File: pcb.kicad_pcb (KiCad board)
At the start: 4 copper layers, 65 x 56 mm, 28 parts, among them J1 230VAC IN, J10 DHT22 2, J11 DHT22 3, J12 LIGHTS, J2 12VDC IN, J3 40HAT, J4 CONN_01X02, J5 CONN_02X02, J6 FAN 1, J7 FAN 2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

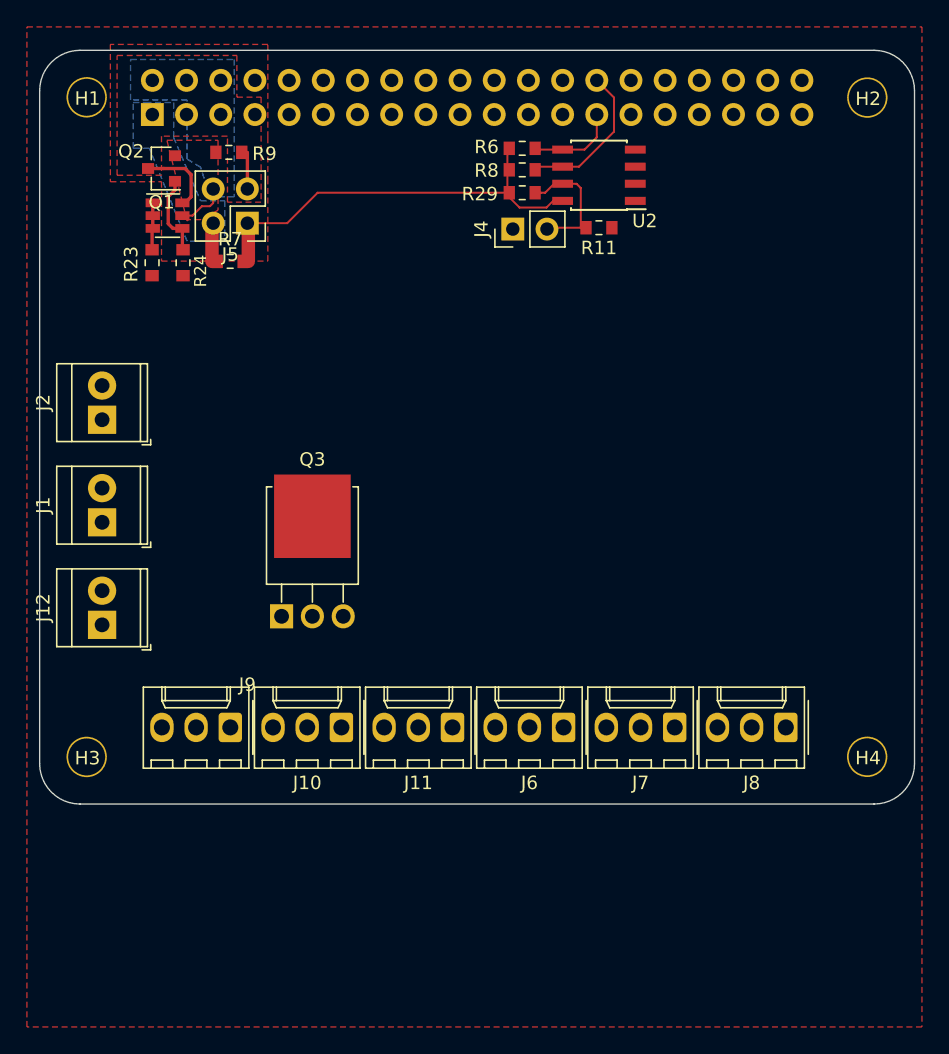
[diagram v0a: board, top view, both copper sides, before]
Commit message: Rearranged connectors. Added early triac circuit.
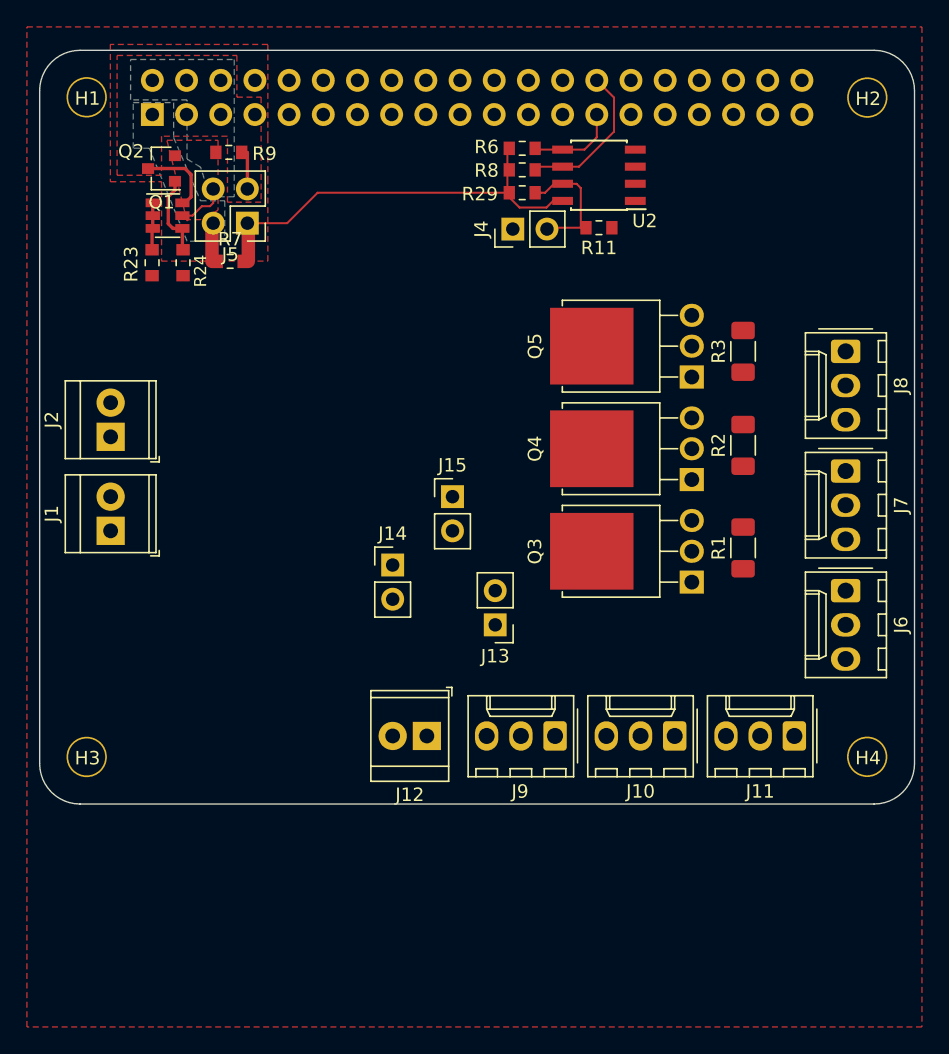
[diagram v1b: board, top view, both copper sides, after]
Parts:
- added J13: Conn_01x02, Connector_PinHeader_2.54mm:PinHeader_1x02_P2.54mm_Vertical, F.Cu at (112.4, 103.5)
- added J14: Conn_01x02, Connector_PinHeader_2.54mm:PinHeader_1x02_P2.54mm_Vertical, F.Cu at (104.8, 99.1)
- added J15: Conn_01x02, Connector_PinHeader_2.54mm:PinHeader_1x02_P2.54mm_Vertical, F.Cu at (109.2, 94.0)
- added Q4: IRLU024NPBF, Package_TO_SOT_THT:TO-251-3-1EP_Horizontal_TabDown, F.Cu at (127.0, 92.7)
- added Q5: IRLU024NPBF, Package_TO_SOT_THT:TO-251-3-1EP_Horizontal_TabDown, F.Cu at (127.0, 85.1)
- added R1: 100R, Resistor_SMD:R_1206_3216Metric_Pad1.30x1.75mm_HandSolder, F.Cu at (130.8, 97.8)
- added R2: 100R, Resistor_SMD:R_1206_3216Metric_Pad1.30x1.75mm_HandSolder, F.Cu at (130.8, 90.2)
- added R3: 100R, Resistor_SMD:R_1206_3216Metric_Pad1.30x1.75mm_HandSolder, F.Cu at (130.8, 83.2)
- moved Q3 30.6 mm to (127.0, 100.3), turned to 90 degrees
- moved J8 28.3 mm to (138.4, 83.2), turned to 270 degrees
- moved J12 25.5 mm to (107.3, 111.8), turned to 180 degrees
- moved J11 25.4 mm to (134.6, 111.8)
- moved J10 24.8 mm to (125.7, 111.8)
- moved J9 24.1 mm to (116.8, 111.8)
- moved J6 23.3 mm to (138.4, 101.0), turned to 270 degrees
- moved J7 22.9 mm to (138.4, 92.1), turned to 270 degrees
- moved J2 1.42 mm to (83.8, 89.5)
- moved J1 0.90 mm to (83.8, 96.5)
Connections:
- net Net-(J1-Pad1) renamed /230VAC_L
- net Net-(J1-Pad2) renamed /230VAC_N
- net Net-(J10-Pad2) renamed /DHT22_2_SIGNAL
- net Net-(J11-Pad2) renamed /DHT22_3_SIGNAL
- net Net-(J12-Pad1) renamed /LIGHTS_L
- net Net-(J12-Pad2) renamed /LIGHTS_N
- net Net-(J9-Pad2) renamed /DHT22_1_SIGNAL
- J10 pad 1: Net-(J10-Pad1) -> GND
- J10 pad 3: Net-(J10-Pad3) -> /3.3V
- J11 pad 1: Net-(J11-Pad1) -> GND
- J11 pad 3: Net-(J11-Pad3) -> /3.3V
- J2 pad 1: Net-(J2-Pad1) -> /12VDC
- J2 pad 2: Net-(J2-Pad2) -> GND
- J6 pad 1: Net-(J6-Pad1) -> /FAN_1_OUT
- J6 pad 2: Net-(J6-Pad2) -> /12VDC
- J6 pad 3: Net-(J6-Pad3) -> /FAN_1_RPMa
- J7 pad 1: Net-(J7-Pad1) -> /FAN_2_OUT
- J7 pad 2: Net-(J7-Pad2) -> /12VDC
- J7 pad 3: Net-(J7-Pad3) -> /FAN_2_RPMa
- J8 pad 1: Net-(J8-Pad1) -> /FAN_3_OUT
- J8 pad 2: Net-(J8-Pad2) -> /12VDC
- J8 pad 3: Net-(J8-Pad3) -> /FAN_3_RPMa
- J9 pad 1: Net-(J9-Pad1) -> GND
- J9 pad 3: Net-(J9-Pad3) -> /3.3V
- Q3 pad 2: Net-(Q3-Pad2) -> /FAN_1_OUT
- Q3 pad 3: Net-(Q3-Pad3) -> GND

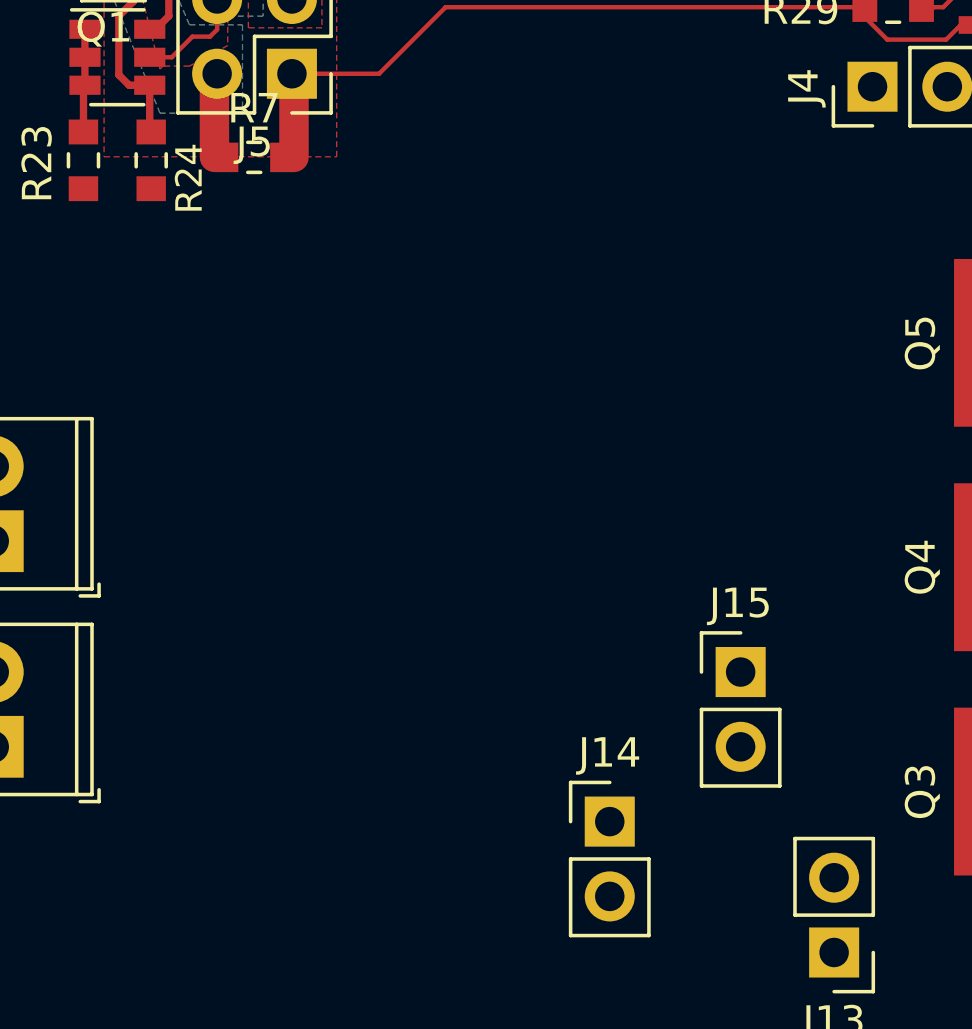
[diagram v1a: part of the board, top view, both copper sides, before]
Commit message: Set optoisolator and triac footprints
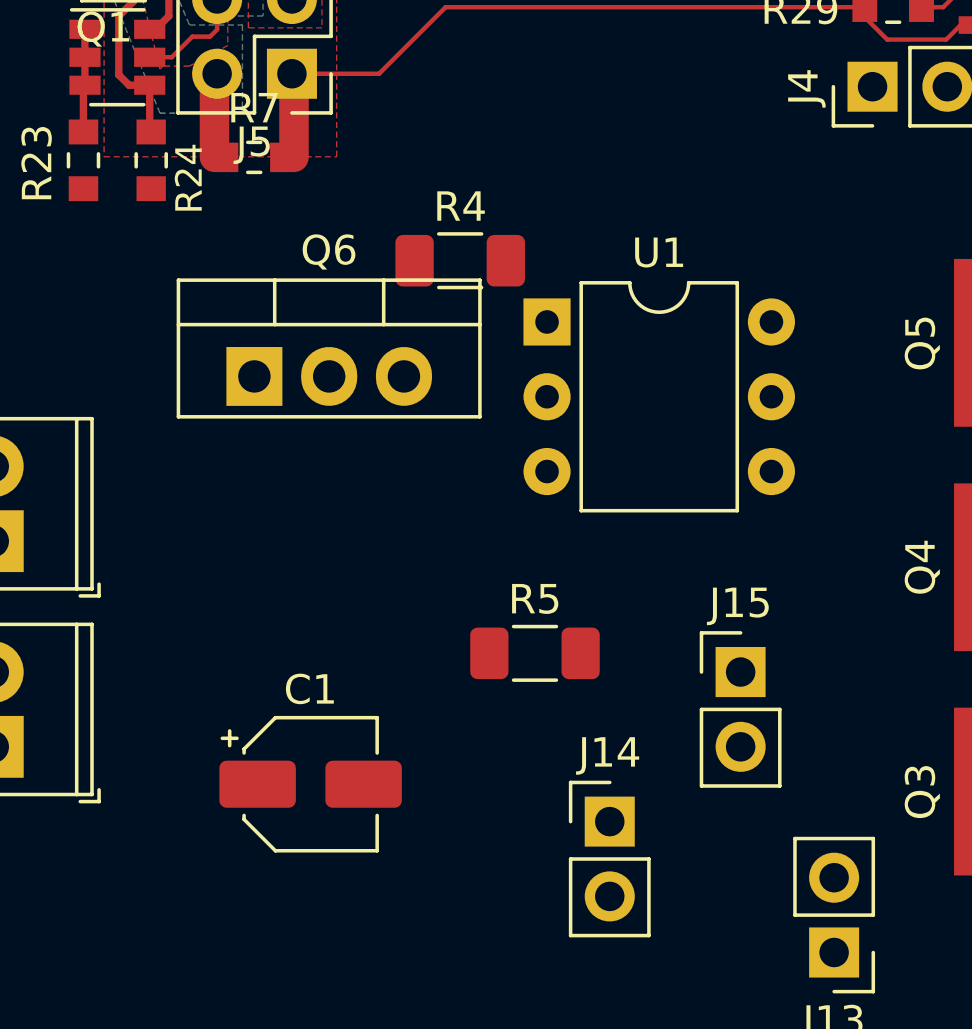
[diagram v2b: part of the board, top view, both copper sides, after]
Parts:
- added C1: 10u, Capacitor_SMD:CP_Elec_4x5.3, F.Cu at (94.6, 97.8)
- added Q6: BT136-600, Package_TO_SOT_THT:TO-220-3_Vertical, F.Cu at (92.7, 83.9)
- added R4: 400R, Resistor_SMD:R_1206_3216Metric_Pad1.30x1.75mm_HandSolder, F.Cu at (99.7, 80.0)
- added R5: 400R, Resistor_SMD:R_1206_3216Metric_Pad1.30x1.75mm_HandSolder, F.Cu at (102.2, 93.3)
- added U1: MOC3043M, Package_DIP:DIP-6_W7.62mm, F.Cu at (102.6, 82.1)
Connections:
- J12 pad 2: /LIGHTS_N -> /230VAC_N

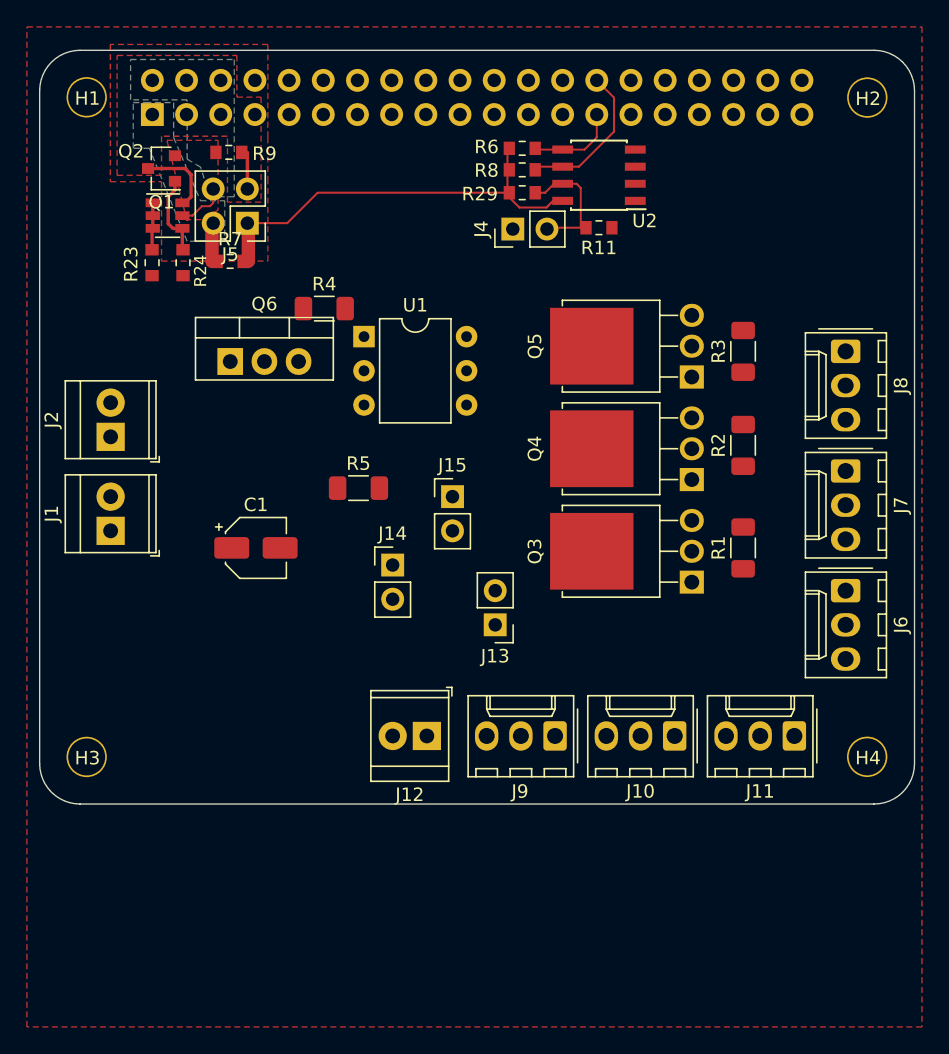
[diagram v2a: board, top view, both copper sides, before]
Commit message: Connect devices to the RPi connector
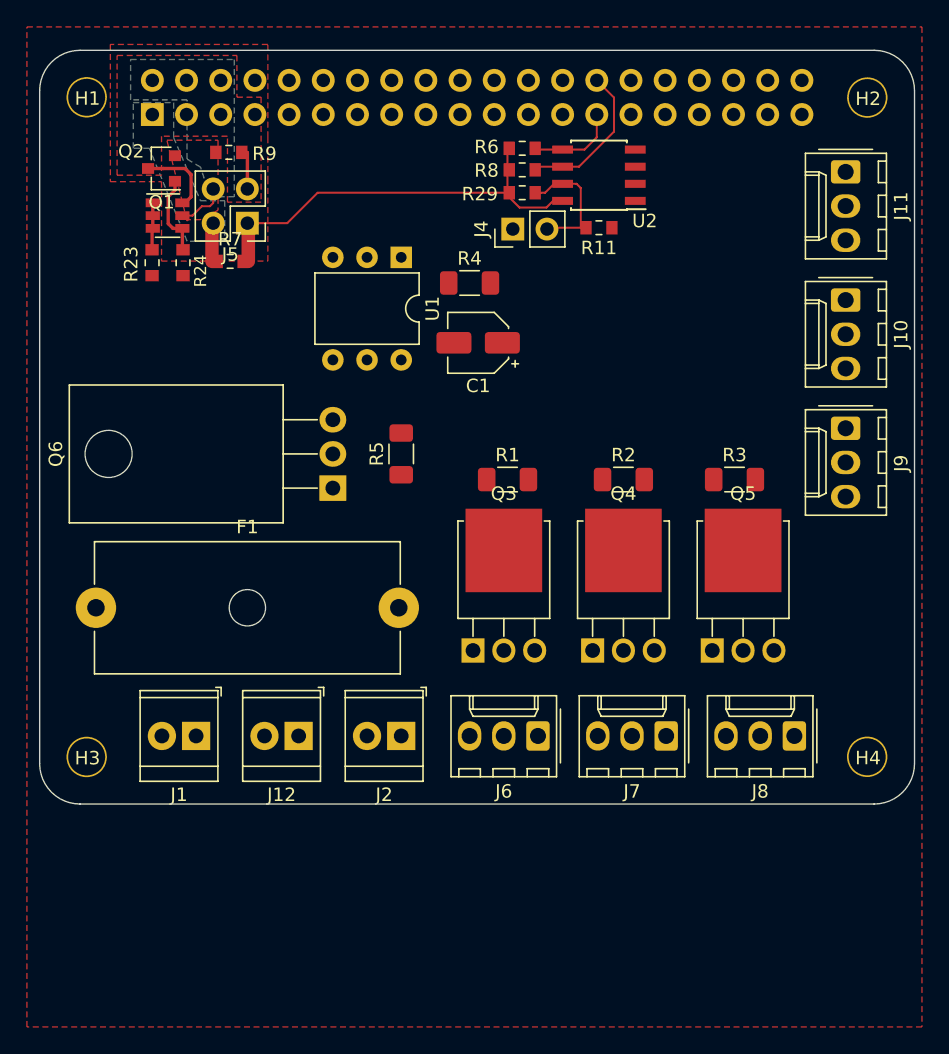
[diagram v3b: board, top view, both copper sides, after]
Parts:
- removed J13, J14, J15: Conn_01x02, Connector_PinHeader_2.54mm:PinHeader_1x02_P2.54mm_Vertical
- added F1: 1A, Fuse:Fuseholder_Cylinder-5x20mm_Schurter_0031_8201_Horizontal_Open, F.Cu at (82.7, 102.2)
- Q6: footprint Package_TO_SOT_THT:TO-220-3_Vertical -> Package_TO_SOT_THT:TO-220-3_Horizontal_TabDown
- R4: value 400R -> 560R
- R5: value 400R -> 22R
- moved J11 42.1 mm to (138.4, 69.8), turned to 270 degrees
- moved J10 34.8 mm to (138.4, 79.4), turned to 270 degrees
- moved J9 31.4 mm to (138.4, 88.9), turned to 270 degrees
- moved J2 31.0 mm to (105.4, 111.8), turned to 180 degrees
- moved J8 28.8 mm to (134.6, 111.8), turned to 180 degrees
- moved J6 25.3 mm to (115.6, 111.8), turned to 180 degrees
- moved J7 23.8 mm to (125.1, 111.8), turned to 180 degrees
- moved C1 22.5 mm to (111.1, 82.5), turned to 180 degrees
- moved Q5 20.4 mm to (128.5, 105.4), turned to 0 degrees
- moved R1 18.2 mm to (113.3, 92.7), turned to 0 degrees
- moved Q3 17.0 mm to (110.7, 105.4), turned to 0 degrees
- moved J1 16.5 mm to (90.2, 111.8), turned to 180 degrees
- moved Q4 14.7 mm to (119.6, 105.4), turned to 0 degrees
- moved Q6 12.1 mm to (100.3, 93.3), turned to 90 degrees
- moved R4 11.0 mm to (110.5, 78.1)
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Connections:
- C1 pad 1: Net-(C1-Pad1) -> /LIGHTS_CONTROL
- C1 pad 2: Net-(C1-Pad2) -> GND
- J3 pad 15: Net-(J3-Pad15) -> /LIGHTS_CONTROL
- J3 pad 16: Net-(J3-Pad16) -> /FAN_1_CONTROL
- J3 pad 18: Net-(J3-Pad18) -> /FAN_2_CONTROL
- J3 pad 22: Net-(J3-Pad22) -> /FAN_3_CONTROL
- J3 pad 31: Net-(J3-Pad31) -> /DHT22_1_SIGNAL
- J3 pad 33: Net-(J3-Pad33) -> /DHT22_2_SIGNAL
- J3 pad 37: Net-(J3-Pad37) -> /DHT22_3_SIGNAL
- J6 pad 3: /FAN_1_RPMa -> /FAN_1_RPM
- J7 pad 3: /FAN_2_RPMa -> /FAN_2_RPM
- J8 pad 3: /FAN_3_RPMa -> /FAN_3_RPM
- Q6 pad 2: /230VAC_L -> Net-(F1-Pad2)
- R4 pad 2: Net-(C1-Pad1) -> /LIGHTS_CONTROL
- R5 pad 1: /230VAC_L -> Net-(F1-Pad2)
- U1 pad 2: Net-(C1-Pad2) -> GND

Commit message: Connect devices 3.3V to HAT's 3.3V
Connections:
- J3 pad 1: /P3V3_HAT -> /3.3V
- J5 pad 2: /P3V3_HAT -> /3.3V
- R7 pad 1: /P3V3_HAT -> /3.3V
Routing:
- net /P3V3_HAT: track 2.88 -> 0.00 mm
- net /3.3V: track 0.00 -> 2.88 mm
- added copper zone on B.Cu, net /3.3V
- removed copper zone on B.Cu, net /P3V3_HAT
